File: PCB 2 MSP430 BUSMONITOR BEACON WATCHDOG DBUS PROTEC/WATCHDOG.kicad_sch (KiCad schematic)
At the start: 12 parts, among them SW1 KMR231NG LFS, SW2 KMR231NG LFS, U2 MAX706RESA, U3 MAX706RESA

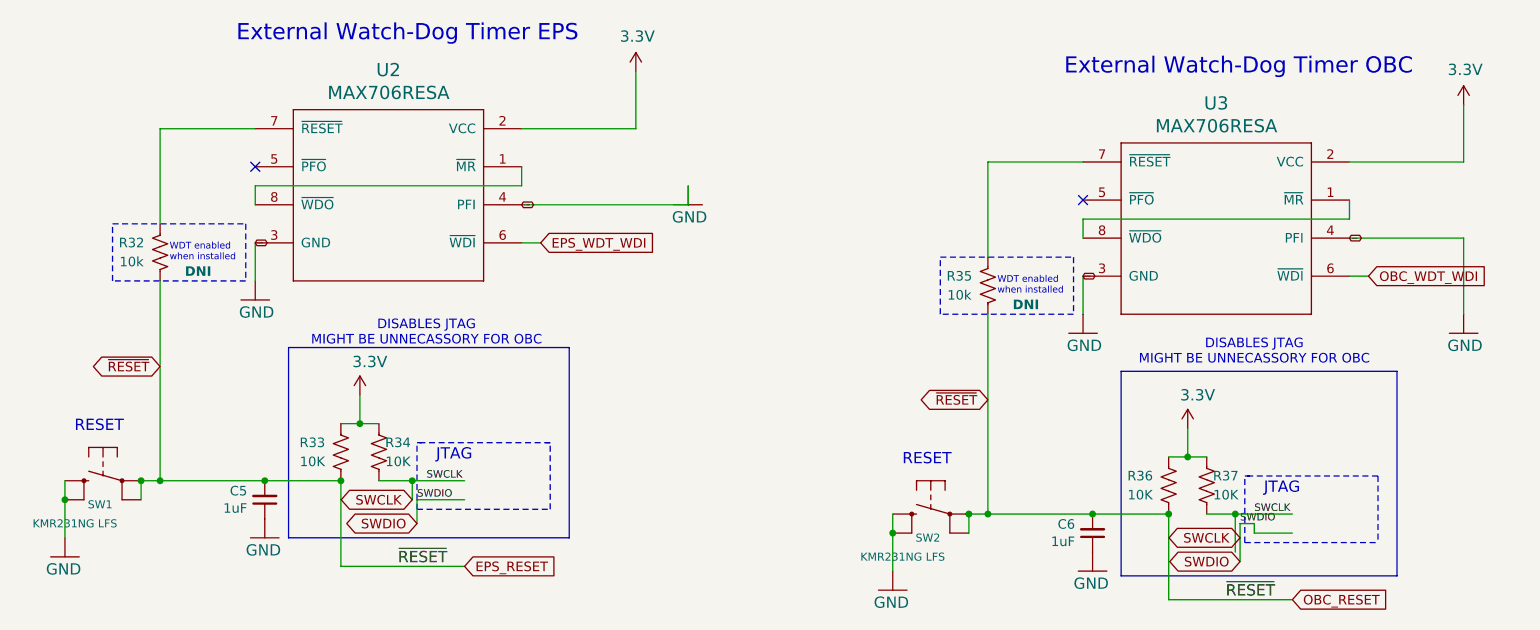
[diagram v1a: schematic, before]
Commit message: Redisgnated components in PCB2 to make more sense
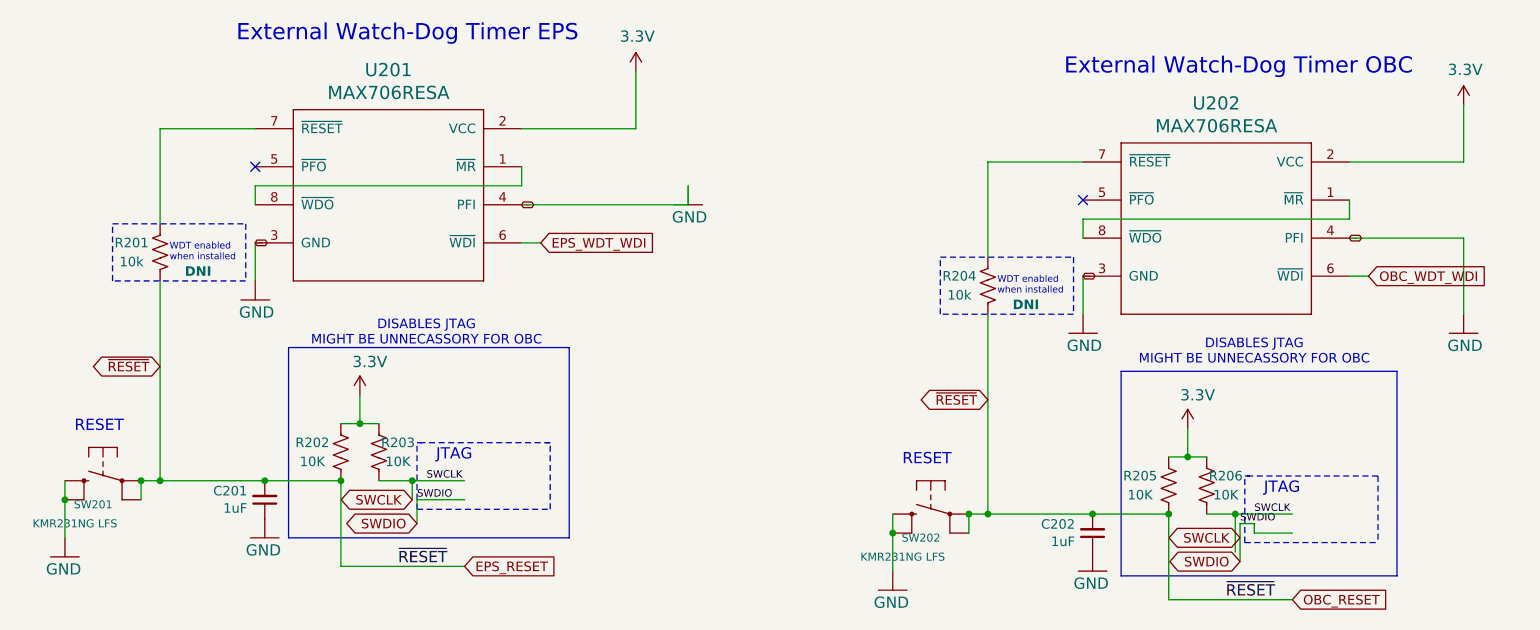
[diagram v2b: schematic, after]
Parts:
- renumbered C5 to C201, C6 to C202, R32 to R201, R33 to R202, R34 to R203, R35 to R204, R36 to R205, R37 to R206, SW1 to SW201, SW2 to SW202, U2 to U201, U3 to U202
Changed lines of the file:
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@@
 		(on_board yes)
 		(dnp no)
-		(property "Reference" "R36"
+		(property "Reference" "R205"
 			(at 196.215 95.885 0)
 			(effects
@@
 			(project "PCB 2 MSP430 BUSMONITOR BEACON WATCHDOG DBUS PROTEC"
 				(path "/04a95c0c-1f2d-49e4-8823-3428ac263eb8/e1e4a250-dfe0-434b-9772-2ee5cbdca3c6"
-					(reference "R36")
+					(reference "R205")
 					(unit 1)
 				)
@@
 		(on_board yes)
 		(dnp no)
-		(property "Reference" "SW2"
+		(property "Reference" "SW202"
 			(at 169.545 104.775 0)
 			(effects
@@
 			(project "PCB 2 MSP430 BUSMONITOR BEACON WATCHDOG DBUS PROTEC"
 				(path "/04a95c0c-1f2d-49e4-8823-3428ac263eb8/e1e4a250-dfe0-434b-9772-2ee5cbdca3c6"
-					(reference "SW2")
+					(reference "SW202")
 					(unit 1)
 				)
@@
 		(on_board yes)
 		(dnp no)
-		(property "Reference" "R34"
+		(property "Reference" "R203"
 			(at 97.155 91.44 0)
 			(effects
@@
 			(project "PCB 2 MSP430 BUSMONITOR BEACON WATCHDOG DBUS PROTEC"
 				(path "/04a95c0c-1f2d-49e4-8823-3428ac263eb8/e1e4a250-dfe0-434b-9772-2ee5cbdca3c6"
-					(reference "R34")
+					(reference "R203")
 					(unit 1)
 				)
@@
 		(on_board yes)
 		(dnp no)
-		(property "Reference" "R35"
+		(property "Reference" "R204"
 			(at 172.085 69.215 0)
 			(effects
@@
 			(project "PCB 2 MSP430 BUSMONITOR BEACON WATCHDOG DBUS PROTEC"
 				(path "/04a95c0c-1f2d-49e4-8823-3428ac263eb8/e1e4a250-dfe0-434b-9772-2ee5cbdca3c6"
-					(reference "R35")
+					(reference "R204")
 					(unit 1)
 				)
@@
 		(on_board yes)
 		(dnp no)
-		(property "Reference" "R37"
+		(property "Reference" "R206"
 			(at 207.645 95.885 0)
 			(effects
@@
 			(project "PCB 2 MSP430 BUSMONITOR BEACON WATCHDOG DBUS PROTEC"
 				(path "/04a95c0c-1f2d-49e4-8823-3428ac263eb8/e1e4a250-dfe0-434b-9772-2ee5cbdca3c6"
-					(reference "R37")
+					(reference "R206")
 					(unit 1)
 				)
@@
 		(on_board yes)
 		(dnp no)
-		(property "Reference" "R33"
+		(property "Reference" "R202"
 			(at 85.725 91.44 0)
 			(effects
@@
 			(project "PCB 2 MSP430 BUSMONITOR BEACON WATCHDOG DBUS PROTEC"
 				(path "/04a95c0c-1f2d-49e4-8823-3428ac263eb8/e1e4a250-dfe0-434b-9772-2ee5cbdca3c6"
-					(reference "R33")
+					(reference "R202")
 					(unit 1)
 				)
@@
 		(on_board yes)
 		(dnp no)
-		(property "Reference" "U2"
+		(property "Reference" "U201"
 			(at 95.885 41.7068 0)
 			(effects
@@
 			(project "PCB 2 MSP430 BUSMONITOR BEACON WATCHDOG DBUS PROTEC"
 				(path "/04a95c0c-1f2d-49e4-8823-3428ac263eb8/e1e4a250-dfe0-434b-9772-2ee5cbdca3c6"
-					(reference "U2")
+					(reference "U201")
 					(unit 1)
 				)
@@
 		(on_board yes)
 		(dnp no)
-		(property "Reference" "C5"
+		(property "Reference" "C201"
 			(at 77.0382 97.8916 0)
 			(effects
@@
 			(project "PCB 2 MSP430 BUSMONITOR BEACON WATCHDOG DBUS PROTEC"
 				(path "/04a95c0c-1f2d-49e4-8823-3428ac263eb8/e1e4a250-dfe0-434b-9772-2ee5cbdca3c6"
-					(reference "C5")
+					(reference "C201")
 					(unit 1)
 				)
@@
 		(on_board yes)
 		(dnp no)
-		(property "Reference" "R32"
+		(property "Reference" "R201"
 			(at 61.595 64.77 0)
 			(effects
@@
 			(project "PCB 2 MSP430 BUSMONITOR BEACON WATCHDOG DBUS PROTEC"
 				(path "/04a95c0c-1f2d-49e4-8823-3428ac263eb8/e1e4a250-dfe0-434b-9772-2ee5cbdca3c6"
-					(reference "R32")
+					(reference "R201")
 					(unit 1)
 				)
@@
 		(on_board yes)
 		(dnp no)
-		(property "Reference" "SW1"
+		(property "Reference" "SW201"
 			(at 59.055 100.33 0)
 			(effects
@@
 			(project "PCB 2 MSP430 BUSMONITOR BEACON WATCHDOG DBUS PROTEC"
 				(path "/04a95c0c-1f2d-49e4-8823-3428ac263eb8/e1e4a250-dfe0-434b-9772-2ee5cbdca3c6"
-					(reference "SW1")
+					(reference "SW201")
 					(unit 1)
 				)
@@
 		(on_board yes)
 		(dnp no)
-		(property "Reference" "C6"
+		(property "Reference" "C202"
 			(at 187.5282 102.3366 0)
 			(effects
@@
 			(project "PCB 2 MSP430 BUSMONITOR BEACON WATCHDOG DBUS PROTEC"
 				(path "/04a95c0c-1f2d-49e4-8823-3428ac263eb8/e1e4a250-dfe0-434b-9772-2ee5cbdca3c6"
-					(reference "C6")
+					(reference "C202")
 					(unit 1)
 				)
@@
 		(on_board yes)
 		(dnp no)
-		(property "Reference" "U3"
+		(property "Reference" "U202"
 			(at 206.375 46.1518 0)
 			(effects
@@
 			(project "PCB 2 MSP430 BUSMONITOR BEACON WATCHDOG DBUS PROTEC"
 				(path "/04a95c0c-1f2d-49e4-8823-3428ac263eb8/e1e4a250-dfe0-434b-9772-2ee5cbdca3c6"
-					(reference "U3")
-					(unit 1)
-				)
+					(reference "U202")
+					(unit 1)
+				)

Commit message: Signed-off-by: ARYANTECH123 <ateamxxx101@gmail.com>
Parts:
- removed R205, R206: 10K, Resistor_SMD:R_0603_1608Metric, symbol Device:R_US
- removed SW201, SW202: KMR231NG LFS, mainboard:BTN_KMR2_4.6X2.8, symbol mainboard:SWITCH_SMT4.6X2.8
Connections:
- net EPS_RESET: no longer C202.2, R204.1
- new net OBC_RESET: C202.2, R204.1
